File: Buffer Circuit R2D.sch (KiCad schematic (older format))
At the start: 20 parts, among them Q13 Q_NPN_BCE, Q14 Q_PNP_BCE, Q15 Q_NPN_BCE, Q16 Q_PNP_BCE, U10 AD8664ARZ

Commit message: continued R2D AS1200 has encoder-interface
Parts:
- removed Q13, Q15: Q_NPN_BCE, Package_TO_SOT_SMD:SOT-23, symbol Amalga_100-rescue:Q_NPN_BCE-Device
- removed Q14, Q16: Q_PNP_BCE, Package_TO_SOT_SMD:SOT-23, symbol Amalga_100-rescue:Q_PNP_BCE-Device
- added C37: 100nF, Capacitor_SMD:C_0805_2012Metric, symbol Amalga_100-rescue:C_Small-Device
- added C? (x2): 120pF, Capacitor_SMD:C_0805_2012Metric, symbol Amalga_100-rescue:C_Small-Device
- added Q13, Q15: BC846B, Package_TO_SOT_SMD:SOT-23, symbol Transistor_BJT:BC847
- added Q14, Q16: BC856B, Package_TO_SOT_SMD:SOT-23, symbol Device:Q_PNP_BEC
- added R? (x2): 15k4, Resistor_SMD:R_0805_2012Metric, symbol Amalga_100-rescue:R_Small-Device
- gave numbers to parts that had none: 1
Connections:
- wire segments 62 -> 73
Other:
- note added: "Filter"
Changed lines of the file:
@@
 	3700 3450 3700 1800
-$Comp
-L Amalga_100-rescue:Q_NPN_BCE-Device Q?
-U 1 1 5CC00953
-P 6550 2500
-AR Path="/5C9D0FFC/5CC00953" Ref="Q?"  Part="1"
-AR Path="/5C9D0FFC/5CBFECD2/5CC00953" Ref="Q13"  Part="1"
-AR Path="/5CC00953" Ref="Q13"  Part="1"
-F 0 "Q13" H 6741 2546 50  0000 L CNN
-F 1 "Q_NPN_BCE" H 6741 2455 50  0000 L CNN
-F 2 "Package_TO_SOT_SMD:SOT-23" H 6750 2600 50  0001 C CNN
-F 3 "~" H 6550 2500 50  0001 C CNN
-	1    6550 2500
-	1    0    0    -1
-$EndComp
-$Comp
-L Amalga_100-rescue:Q_PNP_BCE-Device Q?
-U 1 1 5CC0095A
-P 6550 3300
-AR Path="/5C9D0FFC/5CC0095A" Ref="Q?"  Part="1"
-AR Path="/5C9D0FFC/5CBFECD2/5CC0095A" Ref="Q14"  Part="1"
-F 0 "Q14" H 6741 3346 50  0000 L CNN
-F 1 "Q_PNP_BCE" H 6741 3255 50  0000 L CNN
-F 2 "Package_TO_SOT_SMD:SOT-23" H 6750 3400 50  0001 C CNN
-F 3 "~" H 6550 3300 50  0001 C CNN
-	1    6550 3300
-	1    0    0    1
-$EndComp
 $Comp
 L Amalga_100-rescue:R_Small-Device R?
@@
 Wire Wire Line
 	7450 1800 7450 2900
-Wire Wire Line
-	3700 1800 7450 1800
 Connection ~ 7450 2900
 Wire Wire Line
@@
 	5550 2850 6150 2850
 $Comp
-L Amalga_100-rescue:Q_NPN_BCE-Device Q?
-U 1 1 5CC037D1
-P 9200 2550
-AR Path="/5C9D0FFC/5CC037D1" Ref="Q?"  Part="1"
-AR Path="/5C9D0FFC/5CBFECD2/5CC037D1" Ref="Q15"  Part="1"
-AR Path="/5CC037D1" Ref="Q15"  Part="1"
-F 0 "Q15" H 9391 2596 50  0000 L CNN
-F 1 "Q_NPN_BCE" H 9391 2505 50  0000 L CNN
-F 2 "Package_TO_SOT_SMD:SOT-23" H 9400 2650 50  0001 C CNN
-F 3 "~" H 9200 2550 50  0001 C CNN
-	1    9200 2550
-	1    0    0    -1
-$EndComp
-$Comp
-L Amalga_100-rescue:Q_PNP_BCE-Device Q?
-U 1 1 5CC037D8
-P 9200 3350
-AR Path="/5C9D0FFC/5CC037D8" Ref="Q?"  Part="1"
-AR Path="/5C9D0FFC/5CBFECD2/5CC037D8" Ref="Q16"  Part="1"
-F 0 "Q16" H 9391 3396 50  0000 L CNN
-F 1 "Q_PNP_BCE" H 9391 3305 50  0000 L CNN
-F 2 "Package_TO_SOT_SMD:SOT-23" H 9400 3450 50  0001 C CNN
-F 3 "~" H 9200 3350 50  0001 C CNN
-	1    9200 3350
-	1    0    0    1
-$EndComp
-$Comp
 L Amalga_100-rescue:R_Small-Device R?
 U 1 1 5CC037DF
@@
 Wire Wire Line
 	3750 3650 3650 3650
-Wire Wire Line
-	3650 3650 3650 1750
-Wire Wire Line
-	3650 1750 10100 1750
 $Comp
 L Amalga_100-rescue:R_Small-Device R?
@@
 *EXC
 Wire Wire Line
-	10100 1750 10100 2950
-Wire Wire Line
 	3750 3050 3150 3050
 Wire Wire Line
@@
 Connection ~ 3150 2850
 Wire Wire Line
-	3150 2850 1150 2850
+	3150 2850 1600 2850
 Wire Wire Line
 	1150 2800 1150 2850
@@
 P 3350 4100
 AR Path="/5899E25F/5CB0C079" Ref="#PWR?"  Part="1"
-AR Path="/5C9D0FFC/5CBFECD2/5CB0C079" Ref="#PWR?"  Part="1"
-F 0 "#PWR?" H 3350 3950 50  0001 C CNN
+AR Path="/5C9D0FFC/5CBFECD2/5CB0C079" Ref="#PWR0147"  Part="1"
+F 0 "#PWR0147" H 3350 3950 50  0001 C CNN
 F 1 "+15V" H 3365 4273 50  0000 C CNN
 F 2 "" H 3350 4100 50  0001 C CNN
@@
 AR Path="/5895E6A0/5CB0DA45" Ref="C?"  Part="1"
 AR Path="/5C9D0FFC/5CB0DA45" Ref="C?"  Part="1"
-AR Path="/5C9D0FFC/5CBFECD2/5CB0DA45" Ref="C?"  Part="1"
-F 0 "C?" H 3360 4470 50  0000 L CNN
+AR Path="/5C9D0FFC/5CBFECD2/5CB0DA45" Ref="C36"  Part="1"
+F 0 "C36" H 3360 4470 50  0000 L CNN
 F 1 "100nF" H 3360 4320 50  0000 L CNN
 F 2 "Capacitor_SMD:C_0805_2012Metric" H 3350 4400 50  0001 C CNN
@@
 Wire Wire Line
 	3650 4550 3650 4700
+$Comp
+L Amalga_100-rescue:C_Small-Device C?
+U 1 1 5CAF048C
+P 1600 3100
+AR Path="/5895E6A0/5CAF048C" Ref="C?"  Part="1"
+AR Path="/5C9D0FFC/5CAF048C" Ref="C?"  Part="1"
+AR Path="/5C9D0FFC/5CBFECD2/5CAF048C" Ref="C37"  Part="1"
+F 0 "C37" H 1610 3170 50  0000 L CNN
+F 1 "100nF" H 1610 3020 50  0000 L CNN
+F 2 "Capacitor_SMD:C_0805_2012Metric" H 1600 3100 50  0001 C CNN
+F 3 "" H 1600 3100 50  0000 C CNN
+	1    1600 3100
+	1    0    0    -1
+$EndComp
+$Comp
+L Amalga_100-rescue:GND-power #PWR?
+U 1 1 5CAF1766
+P 1600 3300
+AR Path="/5895E6A0/5CAF1766" Ref="#PWR?"  Part="1"
+AR Path="/5C9D0FFC/5CAF1766" Ref="#PWR?"  Part="1"
+AR Path="/5C9D0FFC/5CBFECD2/5CAF1766" Ref="#PWR019"  Part="1"
+F 0 "#PWR019" H 1600 3050 50  0001 C CNN
+F 1 "GND" H 1600 3150 50  0000 C CNN
+F 2 "" H 1600 3300 50  0000 C CNN
+F 3 "" H 1600 3300 50  0000 C CNN
+	1    1600 3300
+	1    0    0    -1
+$EndComp
+Wire Wire Line
+	1600 2850 1600 3000
+Connection ~ 1600 2850
+Wire Wire Line
+	1600 2850 1150 2850
+Wire Wire Line
+	1600 3200 1600 3300
+$Comp
+L Transistor_BJT:BC847 Q13
+U 1 1 5CAF787F
+P 6550 2500
+F 0 "Q13" H 6741 2546 50  0000 L CNN
+F 1 "BC846B" H 6741 2455 50  0000 L CNN
+F 2 "Package_TO_SOT_SMD:SOT-23" H 6750 2425 50  0001 L CIN
+F 3 "http://www.infineon.com/dgdl/Infineon-BC847SERIES_BC848SERIES_BC849SERIES_BC850SERIES-DS-v01_01-en.pdf?fileId=db3a304314dca389011541d4630a1657" H 6550 2500 50  0001 L CNN
+	1    6550 2500
+	1    0    0    -1
+$EndComp
+$Comp
+L Transistor_BJT:BC847 Q15
+U 1 1 5CAF78F8
+P 9200 2550
+F 0 "Q15" H 9391 2596 50  0000 L CNN
+F 1 "BC846B" H 9391 2505 50  0000 L CNN
+F 2 "Package_TO_SOT_SMD:SOT-23" H 9400 2475 50  0001 L CIN
+F 3 "http://www.infineon.com/dgdl/Infineon-BC847SERIES_BC848SERIES_BC849SERIES_BC850SERIES-DS-v01_01-en.pdf?fileId=db3a304314dca389011541d4630a1657" H 9200 2550 50  0001 L CNN
+	1    9200 2550
+	1    0    0    -1
+$EndComp
+$Comp
+L Device:Q_PNP_BEC Q14
+U 1 1 5CAF8F99
+P 6550 3300
+F 0 "Q14" H 6741 3254 50  0000 L CNN
+F 1 "BC856B" H 6741 3345 50  0000 L CNN
+F 2 "Package_TO_SOT_SMD:SOT-23" H 6750 3400 50  0001 C CNN
+F 3 "~" H 6550 3300 50  0001 C CNN
+	1    6550 3300
+	1    0    0    1
+$EndComp
+$Comp
+L Device:Q_PNP_BEC Q16
+U 1 1 5CAF9090
+P 9200 3350
+F 0 "Q16" H 9391 3304 50  0000 L CNN
+F 1 "BC856B" H 9391 3395 50  0000 L CNN
+F 2 "Package_TO_SOT_SMD:SOT-23" H 9400 3450 50  0001 C CNN
+F 3 "~" H 9200 3350 50  0001 C CNN
+	1    9200 3350
+	1    0    0    1
+$EndComp
+$Comp
+L Amalga_100-rescue:R_Small-Device R?
+U 1 1 5CAFB458
+P 3750 1650
+AR Path="/5C9D0FFC/5CAFB458" Ref="R?"  Part="1"
+AR Path="/5C9D0FFC/5CBFECD2/5CAFB458" Ref="R?"  Part="1"
+F 0 "R?" V 3650 1700 50  0000 C CNN
+F 1 "15k4" V 3550 1650 50  0000 C CNN
+F 2 "Resistor_SMD:R_0805_2012Metric" H 3750 1650 50  0001 C CNN
+F 3 "~" H 3750 1650 50  0001 C CNN
+	1    3750 1650
+	0    -1   -1   0
+$EndComp
+$Comp
+L Amalga_100-rescue:C_Small-Device C?
+U 1 1 5CAFB46B
+P 3750 1500
+AR Path="/5895E6A0/5CAFB46B" Ref="C?"  Part="1"
+AR Path="/5C9D0FFC/5CAFB46B" Ref="C?"  Part="1"
+AR Path="/5C9D0FFC/5CBFECD2/5CAFB46B" Ref="C?"  Part="1"
+F 0 "C?" V 3550 1450 50  0000 L CNN
+F 1 "120pF" V 3650 1400 50  0000 L CNN
+F 2 "Capacitor_SMD:C_0805_2012Metric" H 3750 1500 50  0001 C CNN
+F 3 "" H 3750 1500 50  0000 C CNN
+	1    3750 1500
+	0    1    1    0
+$EndComp
+Wire Wire Line
+	3850 1500 3850 1600
+Wire Wire Line
+	3650 1500 3650 1650
+Wire Wire Line
+	3650 1650 3650 3650
+Connection ~ 3650 1650
+Wire Wire Line
+	3850 1600 10100 1600
+Wire Wire Line
+	10100 1600 10100 2950
+Connection ~ 3850 1600
+Wire Wire Line
+	3850 1600 3850 1650
+$Comp
+L Amalga_100-rescue:R_Small-Device R?
+U 1 1 5CB066FB
+P 4350 1850
+AR Path="/5C9D0FFC/5CB066FB" Ref="R?"  Part="1"
+AR Path="/5C9D0FFC/5CBFECD2/5CB066FB" Ref="R?"  Part="1"
+F 0 "R?" V 4250 1900 50  0000 C CNN
+F 1 "15k4" V 4150 1850 50  0000 C CNN
+F 2 "Resistor_SMD:R_0805_2012Metric" H 4350 1850 50  0001 C CNN
+F 3 "~" H 4350 1850 50  0001 C CNN
+	1    4350 1850
+	0    -1   -1   0
+$EndComp
+$Comp
+L Amalga_100-rescue:C_Small-Device C?
+U 1 1 5CB06702
+P 4350 1700
+AR Path="/5895E6A0/5CB06702" Ref="C?"  Part="1"
+AR Path="/5C9D0FFC/5CB06702" Ref="C?"  Part="1"
+AR Path="/5C9D0FFC/5CBFECD2/5CB06702" Ref="C?"  Part="1"
+F 0 "C?" V 4150 1650 50  0000 L CNN
+F 1 "120pF" V 4250 1600 50  0000 L CNN
+F 2 "Capacitor_SMD:C_0805_2012Metric" H 4350 1700 50  0001 C CNN
+F 3 "" H 4350 1700 50  0000 C CNN
+	1    4350 1700
+	0    1    1    0
+$EndComp
+Wire Wire Line
+	4450 1700 4450 1800
+Wire Wire Line
+	4250 1700 4250 1800
+Connection ~ 4450 1800
+Wire Wire Line
+	4450 1800 4450 1850
+Wire Wire Line
+	4450 1800 7450 1800
+Wire Wire Line
+	3700 1800 4250 1800
+Connection ~ 4250 1800
+Wire Wire Line
+	4250 1800 4250 1850
+Text Notes 4850 950  0    79   ~ 0
+Filter
+Wire Notes Line
+	5050 1000 4150 1500
 $EndSCHEMATC

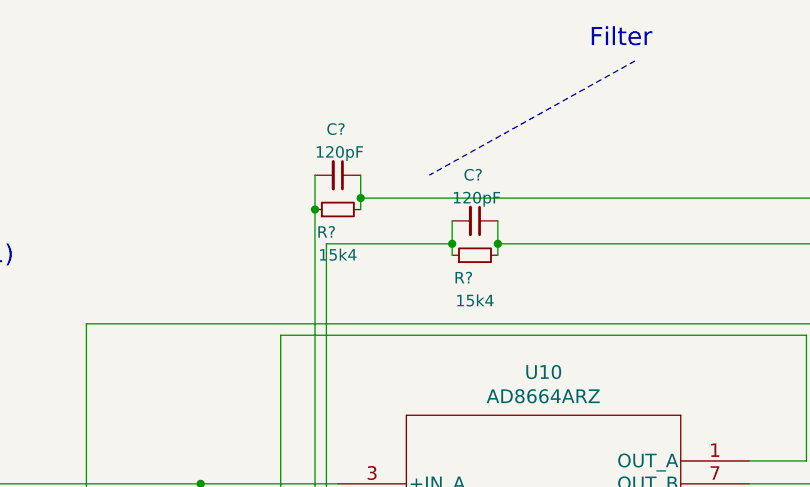
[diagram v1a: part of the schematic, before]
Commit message: continued Resolver continued Routing
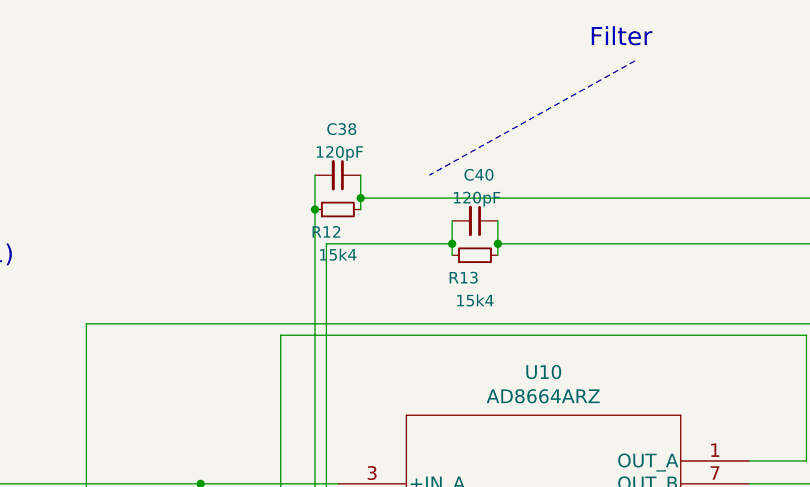
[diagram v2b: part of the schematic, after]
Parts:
- gave numbers to parts that had none: 4
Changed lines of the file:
@@
 $Descr A4 11693 8268
 encoding utf-8
-Sheet 9 10
+Sheet 10 10
 Title ""
 Date ""
@@
 P 3750 1650
 AR Path="/5C9D0FFC/5CAFB458" Ref="R?"  Part="1"
-AR Path="/5C9D0FFC/5CBFECD2/5CAFB458" Ref="R?"  Part="1"
-F 0 "R?" V 3650 1700 50  0000 C CNN
+AR Path="/5C9D0FFC/5CBFECD2/5CAFB458" Ref="R12"  Part="1"
+F 0 "R12" V 3650 1700 50  0000 C CNN
 F 1 "15k4" V 3550 1650 50  0000 C CNN
 F 2 "Resistor_SMD:R_0805_2012Metric" H 3750 1650 50  0001 C CNN
@@
 AR Path="/5895E6A0/5CAFB46B" Ref="C?"  Part="1"
 AR Path="/5C9D0FFC/5CAFB46B" Ref="C?"  Part="1"
-AR Path="/5C9D0FFC/5CBFECD2/5CAFB46B" Ref="C?"  Part="1"
-F 0 "C?" V 3550 1450 50  0000 L CNN
+AR Path="/5C9D0FFC/5CBFECD2/5CAFB46B" Ref="C38"  Part="1"
+F 0 "C38" V 3550 1450 50  0000 L CNN
 F 1 "120pF" V 3650 1400 50  0000 L CNN
 F 2 "Capacitor_SMD:C_0805_2012Metric" H 3750 1500 50  0001 C CNN
@@
 P 4350 1850
 AR Path="/5C9D0FFC/5CB066FB" Ref="R?"  Part="1"
-AR Path="/5C9D0FFC/5CBFECD2/5CB066FB" Ref="R?"  Part="1"
-F 0 "R?" V 4250 1900 50  0000 C CNN
+AR Path="/5C9D0FFC/5CBFECD2/5CB066FB" Ref="R13"  Part="1"
+F 0 "R13" V 4250 1900 50  0000 C CNN
 F 1 "15k4" V 4150 1850 50  0000 C CNN
 F 2 "Resistor_SMD:R_0805_2012Metric" H 4350 1850 50  0001 C CNN
@@
 AR Path="/5895E6A0/5CB06702" Ref="C?"  Part="1"
 AR Path="/5C9D0FFC/5CB06702" Ref="C?"  Part="1"
-AR Path="/5C9D0FFC/5CBFECD2/5CB06702" Ref="C?"  Part="1"
-F 0 "C?" V 4150 1650 50  0000 L CNN
+AR Path="/5C9D0FFC/5CBFECD2/5CB06702" Ref="C40"  Part="1"
+F 0 "C40" V 4150 1650 50  0000 L CNN
 F 1 "120pF" V 4250 1600 50  0000 L CNN
 F 2 "Capacitor_SMD:C_0805_2012Metric" H 4350 1700 50  0001 C CNN

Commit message: continued routing, almost finished resolver. todo: -calc resistors for gain (resolver)       -Anfahren ohne encoder signal?!       -12V buffer R2D
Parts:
- Q14, Q16: symbol Device:Q_PNP_BEC -> Amalga_100-rescue:Q_PNP_BEC-Device
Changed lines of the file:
@@
 $EndComp
 $Comp
-L Device:Q_PNP_BEC Q14
+L Amalga_100-rescue:Q_PNP_BEC-Device Q14
 U 1 1 5CAF8F99
 P 6550 3300
@@
 $EndComp
 $Comp
-L Device:Q_PNP_BEC Q16
+L Amalga_100-rescue:Q_PNP_BEC-Device Q16
 U 1 1 5CAF9090
 P 9200 3350

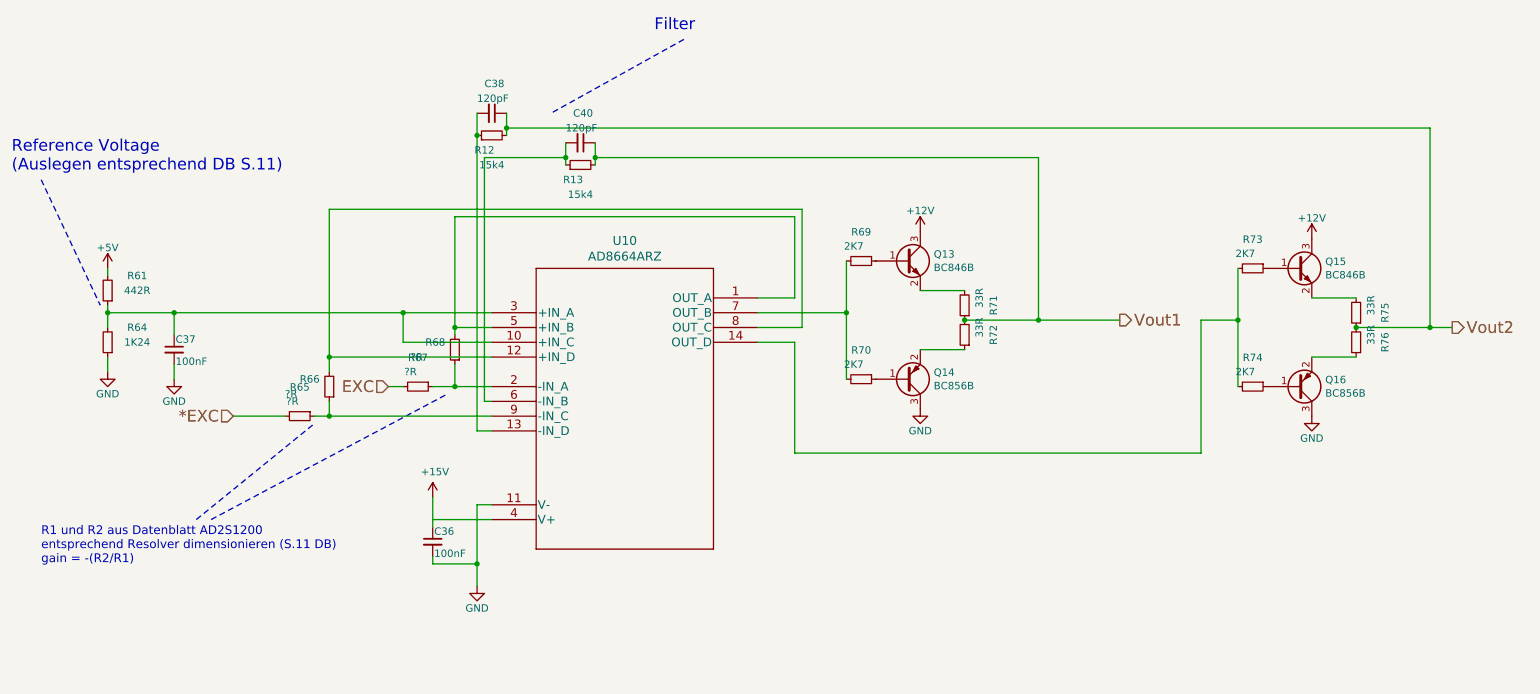
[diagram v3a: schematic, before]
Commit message: -tidied up resolver circuit (need voltage detection on reset pin. >10µs, low active)
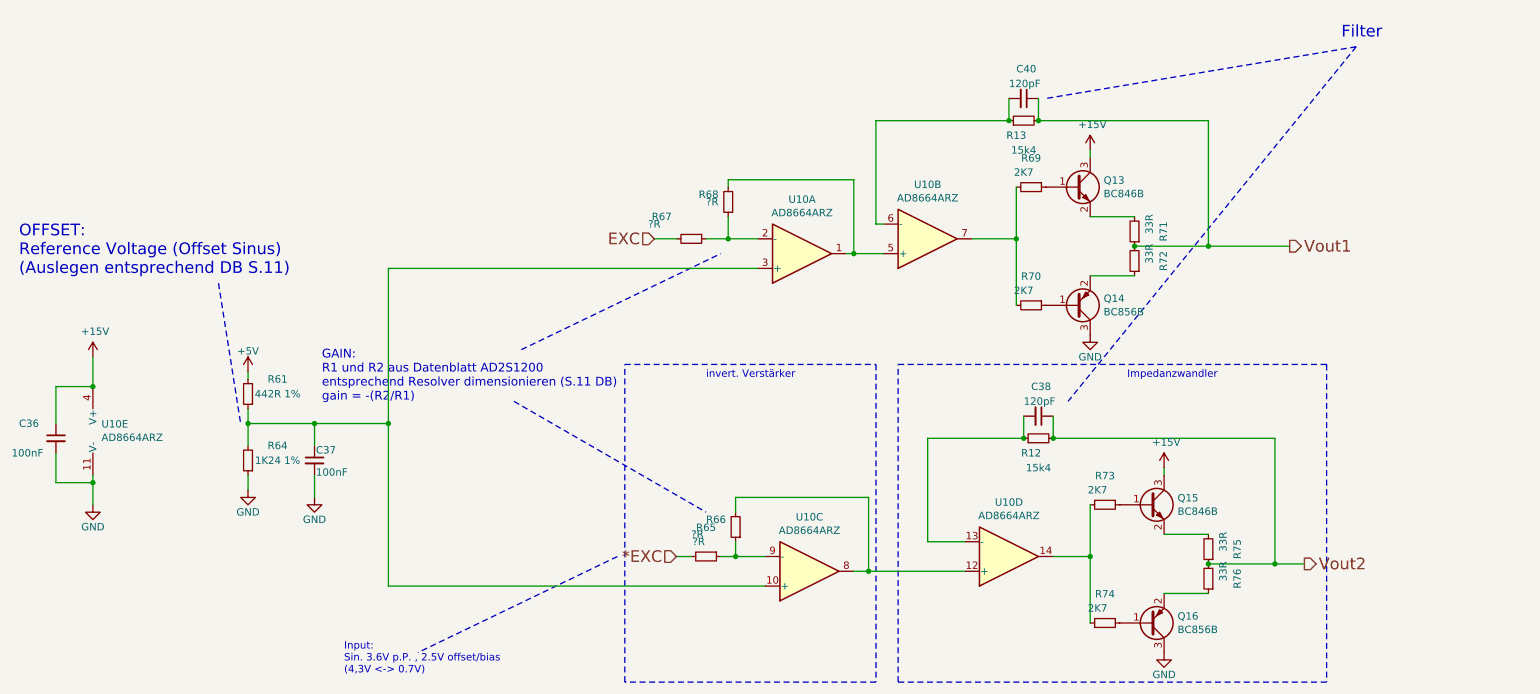
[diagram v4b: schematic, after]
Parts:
- removed U10: AD8664ARZ, Package_SO:SOIC-14_3.9x8.7mm_P1.27mm, symbol Amalga_100-rescue:AD8664ARZ-AD8664ARZ
- added U10: AD8664ARZ, Housings_SOIC:SOIC-14_3.9x8.7mm_Pitch1.27mm, symbol Amplifier_Operational:OPA1604
- R61: value 442R -> 442R 1%
- R64: value 1K24 -> 1K24 1%
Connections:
- net +12V is gone; now on net +15V: Q13.3 (C), Q15.3 (C)
- net +15V: now also U10.4 (V+)
- net GND: now also U10.11 (V-)
- net at C37.1, R61.1, R64.2: now also U10.10 (+), U10.3 (+)
- net at C38.2, R12.1: now also U10.13 (-)
- net at C40.2, R13.1: now also U10.6 (-)
- net at R68.2: now also U10.1, U10.5 (+)
- net at R66.2: now also U10.12 (+), U10.8
- net at R73.2, R74.2: now also U10.14
- net at R67.1, R68.1: now also U10.2 (-)
- net at R69.2, R70.2: now also U10.7
- net at R65.1, R66.1: now also U10.9 (-)
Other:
- note added: "GAIN:\nR1 und R2 aus Datenblatt AD2S1200\nentsprechend Resolver dimensionieren (S.11 DB)\ngain = -(R2/R1)\n\n"
- note added: "Impedanzwandler"
- note added: "Input:\nSin. 3.6V p.P. , 2.5V offset/bias\n(4,3V <-> 0.7V)"
- note added: "OFFSET:\nReference Voltage (Offset Sinus)\n(Auslegen entsprechend DB S.11)\n"
- note added: "invert. Verstärker\n"
- note removed: "R1 und R2 aus Datenblatt AD2S1200\nentsprechend Resolver dimensionieren (S.11 DB)\ngain = -(R2/R1)\n\n"
- note removed: "Reference Voltage\n(Auslegen entsprechend DB S.11)\n"
- moved on the sheet: C36, C37, C38, C40, Q13, Q14, Q15, Q16, R12, R13, R61, R64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

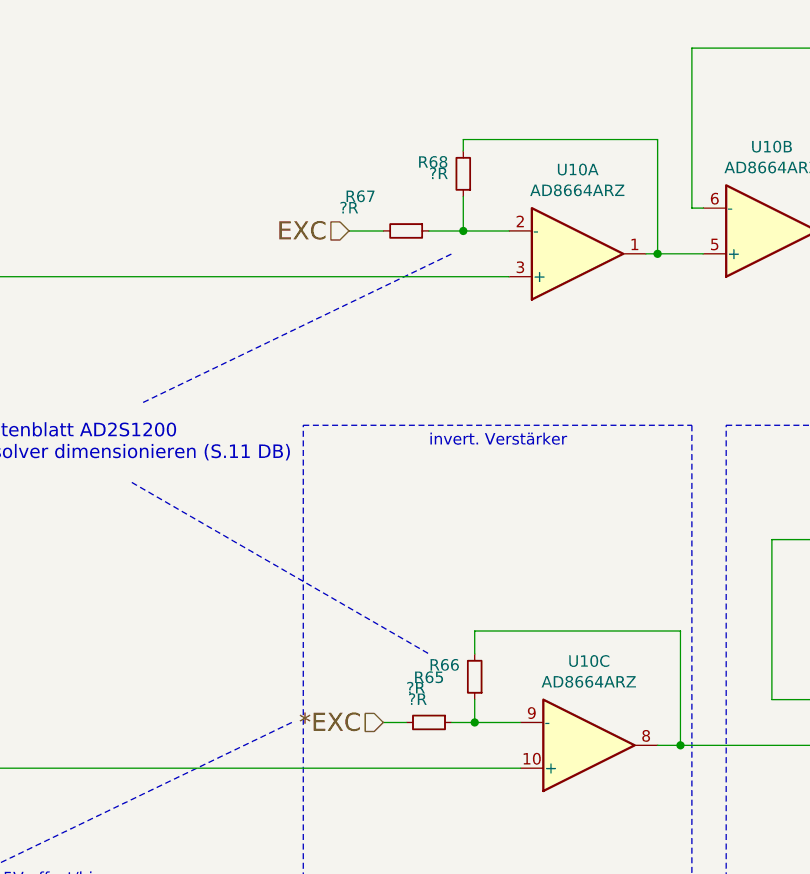
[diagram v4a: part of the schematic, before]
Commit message: -started implementing new sin/cos-Encoder Inputs -small changes like silkscreen
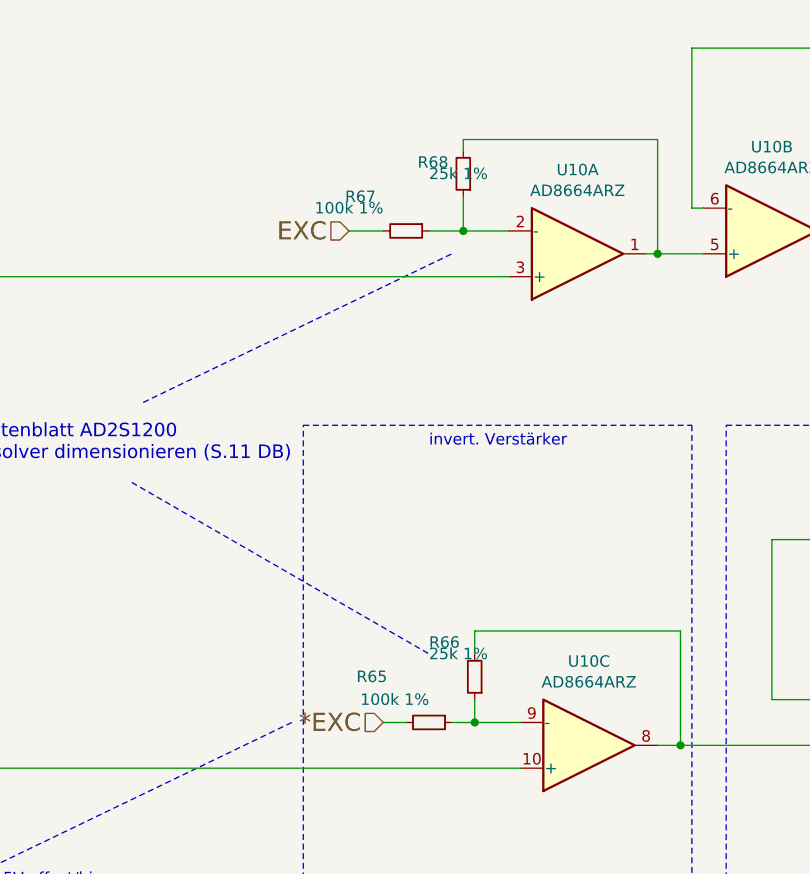
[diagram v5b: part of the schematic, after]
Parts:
- R65, R67: value ?R -> 100k 1%
- R66, R68: value ?R -> 25k 1%
